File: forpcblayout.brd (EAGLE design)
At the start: 95.2 x 66.3 mm, 73 parts, among them J1 3x2 M, J2 S2B-PH-SM4-TB(LF)(SN), J3 629105136821, SW1 AYZ0202AGRLC, SW2 !RESET, T1 2N2222, T2 2N2222, T3 2N2222, T4 2N2222, U1 MCP73831, U2 MIC5219, U3 ATMEGA32U4-AUR, X2 16 MHz

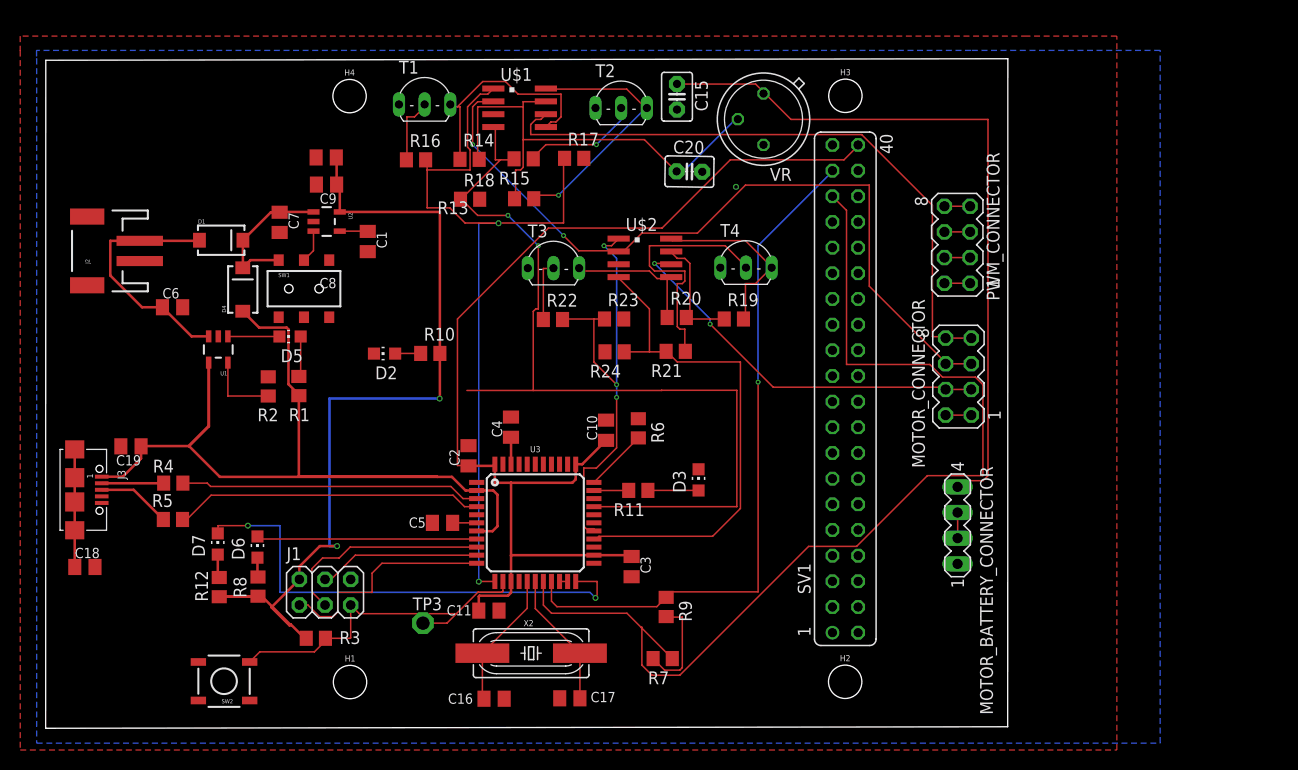
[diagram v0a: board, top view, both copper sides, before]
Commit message: Board tweaks- spacing and right angle approaches to pads
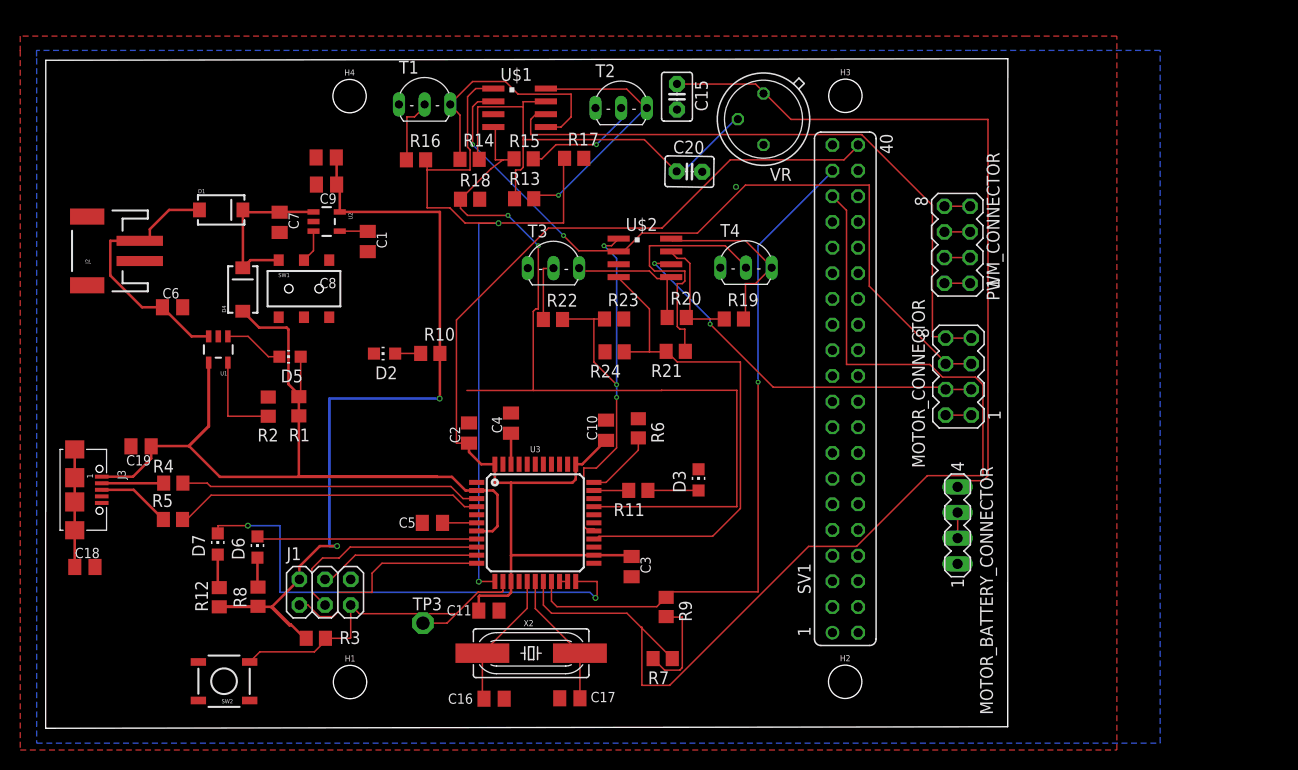
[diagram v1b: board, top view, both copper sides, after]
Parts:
- moved D1 3.00 mm to (17.4, 51.3)
- moved C2 2.25 mm to (41.9, 29.2)
- moved R2 2.00 mm to (22.0, 31.8)
- moved D5 2.00 mm to (24.2, 36.8)
- moved R1 2.00 mm to (25.1, 31.9)
- moved C19 1.00 mm to (9.44, 27.9)
- moved C5 1.00 mm to (38.3, 20.3)
- moved R12 1.00 mm to (17.2, 13.0)
- moved R8 1.00 mm to (21.0, 13.0)
- moved C4 0.40 mm to (46.0, 30.2)
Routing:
- net N$9: track 22.2 -> 25.3 mm
- net SCLK: track 104.0 -> 106.0 mm
- net MCPPROG: track 7.30 -> 9.30 mm
- net PWRIN: track 14.7 -> 16.7 mm
- net V_BATT: track 25.5 -> 27.4 mm
- net UCAP: track 2.38 -> 3.38 mm
- net N$16: track 2.33 -> 3.33 mm
- net N$15: track 1.94 -> 2.94 mm
- net N$4: track 5.11 -> 5.94 mm
- net POWER_IN: track 108.1 -> 107.4 mm
- net PWM_1: track 87.4 -> 88.1 mm
- net PE2/!HWB: track 6.23 -> 6.93 mm
- net PWM_2: track 78.5 -> 79.1 mm

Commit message: Fixed routing mistakes, extended board edge to clear matrix
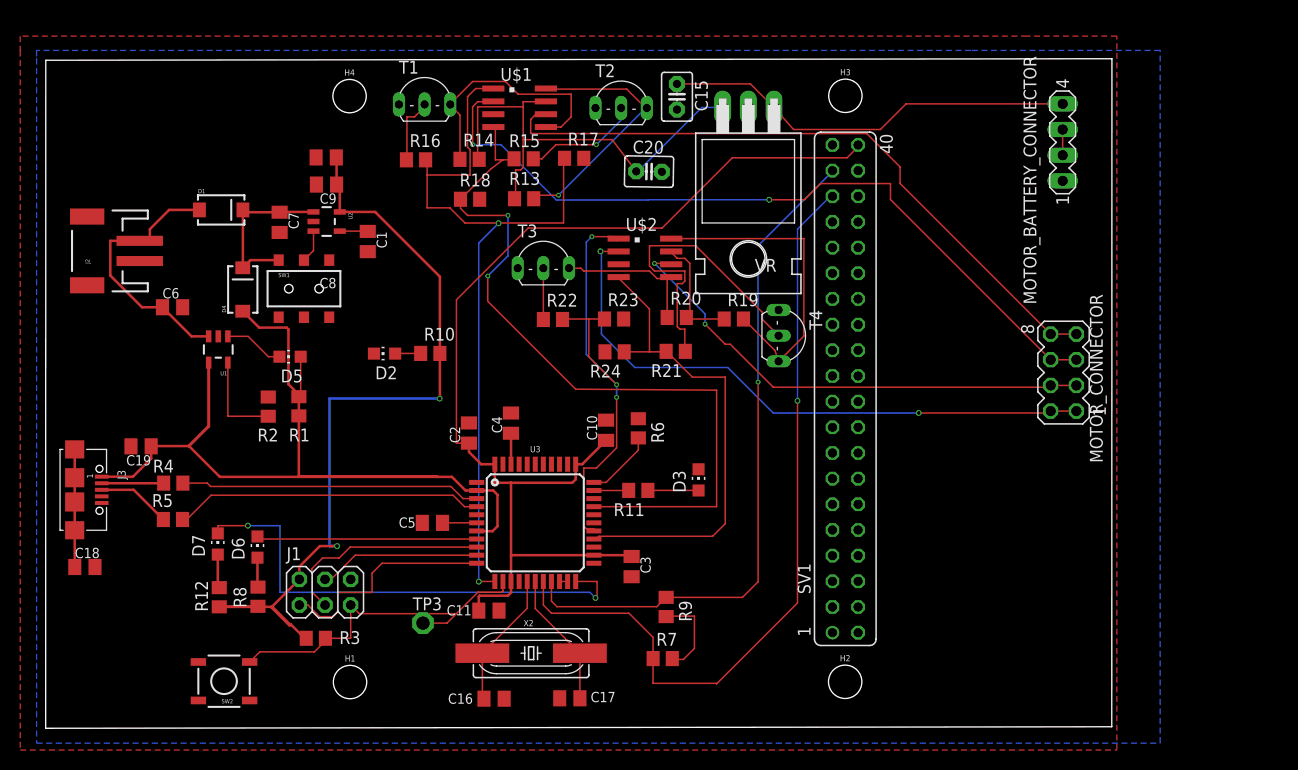
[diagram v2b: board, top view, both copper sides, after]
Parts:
- removed PWM_CONNECTOR: (no value), con-lstb:MA04-2
- VR: device linear:TO39 -> linear:TO220H
- moved MOTOR_BATTERY_CONNECTOR 39.3 mm to (100.6, 58.0)
- moved MOTOR_CONNECTOR 10.4 mm to (100.7, 35.2)
- moved T4 9.18 mm to (73.8, 38.9), turned to 270 degrees
- moved VR 9.12 mm to (69.5, 51.3)
- moved C20 4.00 mm to (59.7, 55.1)
- moved T3 1.00 mm to (49.2, 46.8)
- turned R7 to 0 degrees
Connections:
- removed net N$2: PWM_CONNECTOR.7, PWM_CONNECTOR.8
- removed net N$5: PWM_CONNECTOR.1, PWM_CONNECTOR.2
- removed net N$6: PWM_CONNECTOR.3, PWM_CONNECTOR.4
- removed net N$8: PWM_CONNECTOR.5, PWM_CONNECTOR.6
- net GND: now also VR.2; no longer VR.3
- net H_BRIDGE_POWER: now also VR.3; no longer VR.2
- net LEFT_MOTOR2: no longer U$2.2
- net RIGHT_MOTOR2: now also U$2.2
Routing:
- net RIGHT_MOTOR2: track 2.54 -> 60.7 mm, vias 0 -> 2
- net 7.4V_FROM_BATT: track 71.1 -> 41.2 mm
- net SCLK: track 106.0 -> 78.8 mm, vias 0 -> 1
- net N$18: track 18.1 -> 31.9 mm
- net PWM_1: track 88.1 -> 76.1 mm
- net RIGHT_MOTOR1: track 38.6 -> 49.2 mm
- net N$21: track 25.4 -> 31.8 mm
- net 3.3V: track 86.5 -> 82.7 mm
- net LEFT_MOTOR1: track 62.8 -> 66.3 mm
- net PWM_4: track 45.0 -> 48.2 mm
- net PWM_3: track 50.8 -> 47.8 mm
- net N$8: track 2.54 -> 0.00 mm
- net N$6: track 2.54 -> 0.00 mm
- net N$5: track 2.54 -> 0.00 mm
- net N$2: track 2.54 -> 0.00 mm
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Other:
- board size 95.2 x 66.3 mm -> 105.5 x 66.3 mm

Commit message: Added in 0ohm resistors and added in vias (for stitching)
GND Plane is still a question mark, vias don't seem to be part of flooded planes. Also DRC claims GND pins aren't connected to GND plane
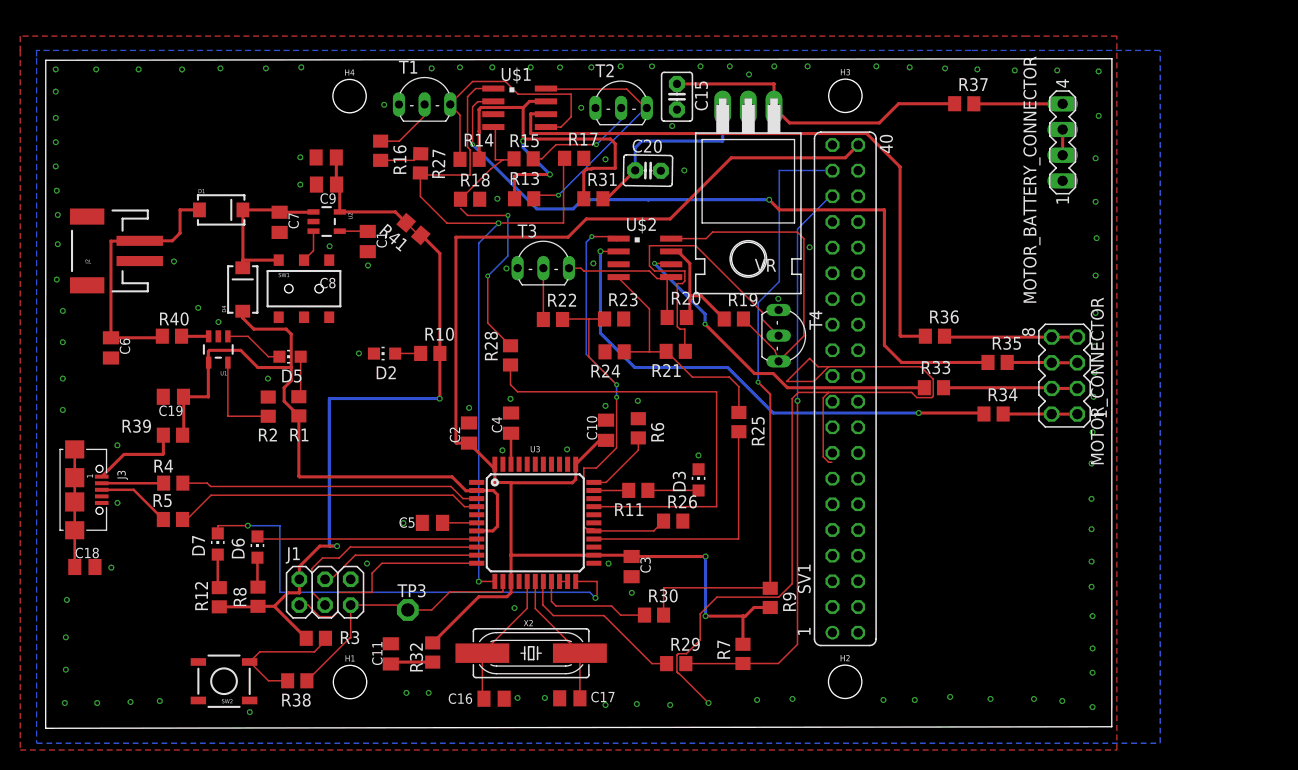
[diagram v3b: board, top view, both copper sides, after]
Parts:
- added R25, R26, R27, R28, R29, R30, R31, R32, R33, R34, R35, R36, R37, R38, R39, R40, R41: 0, rcl:R0805
- moved C11 10.6 mm to (34.2, 7.36), turned to 90 degrees
- moved R9 10.3 mm to (71.7, 12.9)
- moved R7 7.96 mm to (69.0, 7.36), turned to 90 degrees
- moved C6 7.30 mm to (6.46, 37.6), turned to 270 degrees
- moved C19 5.85 mm to (12.6, 32.8)
- moved R16 3.61 mm to (33.1, 57.1), turned to 270 degrees
- moved TP3 1.98 mm to (35.8, 11.7)
- moved MOTOR_CONNECTOR 0.32 mm to (100.8, 34.9)
- moved C20 0.14 mm to (59.6, 55.2)
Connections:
- removed net (5V@2.1A): R7.2, R9.2
- removed net H_BRIDGE_POWER: C20.1, R13.1, R14.2, U$1.7, VR.3
- removed net H_BRIDGE_POWER1: R19.1, R20.2, U$2.7
- new net 7.4_FROM_BATT: C15.1, R37.1, VR.1
- new net ACTUATOR_POWER: C20.1, R19.1, R20.2, R31.2, U$2.7, VR.3
- new net ACUATOR_POWER: R13.1, R14.2, R31.1, U$1.7
- new net N$159: J3.1, R39.2
- new net VBAT: R40.2, U1.3
- net !RESET: now also R38.1, R38.2
- net 3.3V: now also R41.1, R41.2
- net 7.4V_FROM_BATT: now also R37.2; no longer C15.1, VR.1
- net LEFT_MOTOR1: now also R36.1, R36.2
- net LEFT_MOTOR2: now also R35.1, R35.2
- net POWER_IN: now also R32.1, R32.2, R7.2, R9.2
- net PWM_1: now also R28.1, R28.2
- net PWM_2: now also R27.1, R27.2
- net PWM_3: now also R25.1, R25.2
- net PWM_4: now also R26.1, R26.2
- net RIGHT_MOTOR1: now also R33.1, R33.2
- net RIGHT_MOTOR2: now also R34.1, R34.2
- net SCLK: now also R29.1, R29.2
- net SDA: now also R30.1, R30.2
- net VBUS: now also R39.1; no longer J3.1
- net V_BATT: now also R40.1; no longer U1.3
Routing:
- net N$99: track 0.00 -> 85.1 mm, vias 0 -> 1
- net H_BRIDGE_POWER: track 46.3 -> 0.00 mm
- net ACUATOR_POWER: track 0.00 -> 44.2 mm, vias 0 -> 2
- net POWER_IN: track 108.6 -> 144.3 mm, vias 0 -> 2
- net 7.4V_FROM_BATT: track 41.2 -> 8.79 mm
- net ACTUATOR_POWER: track 0.00 -> 31.8 mm
- net 7.4_FROM_BATT: track 0.00 -> 31.2 mm
- net VBUS: track 91.5 -> 66.8 mm
- net H_BRIDGE_POWER1: track 11.8 -> 0.00 mm
- net N$159: track 0.00 -> 8.88 mm
- net (5V@2.1A): track 8.70 -> 0.00 mm
- net LEFT_MOTOR1: track 66.3 -> 73.8 mm
- net PWM_4: track 48.2 -> 55.3 mm
- net SDA: track 67.4 -> 73.2 mm
- net LEFT_MOTOR2: track 77.0 -> 81.5 mm
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
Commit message: Changed 0ohm resistors to through hole
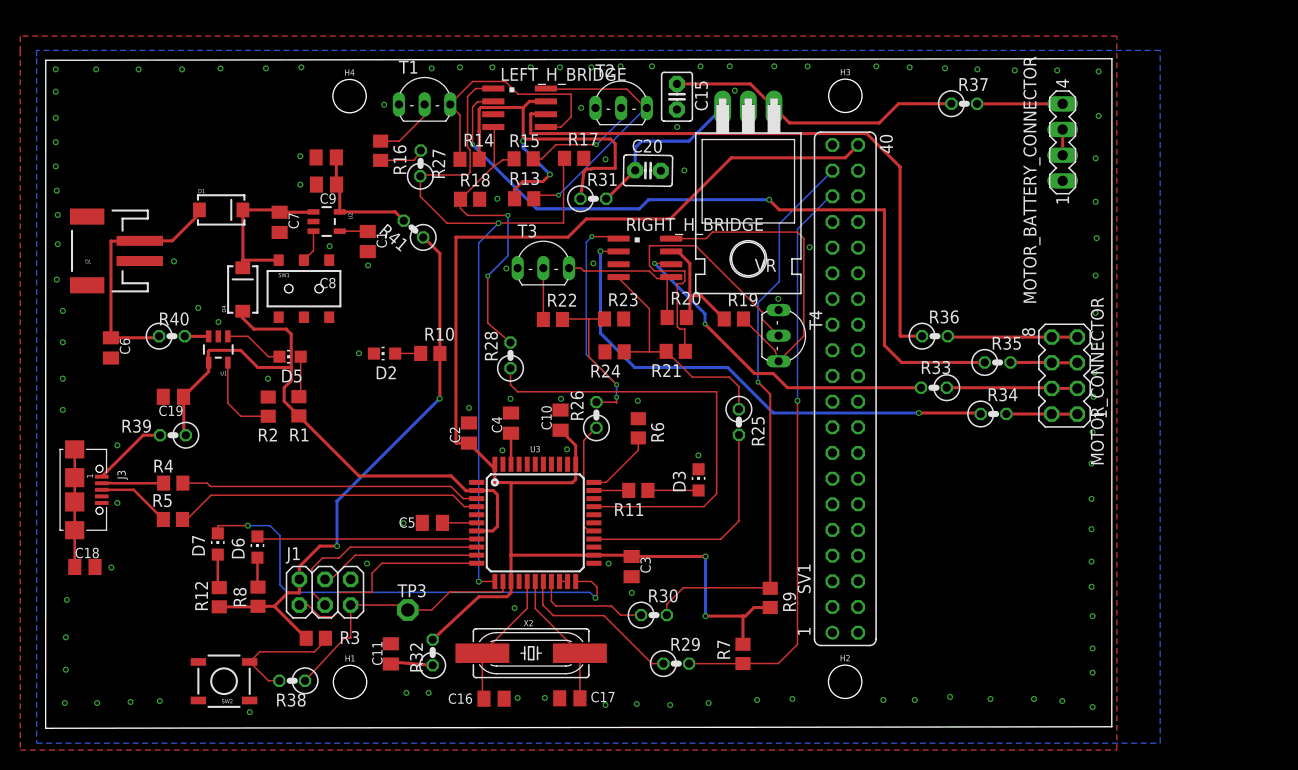
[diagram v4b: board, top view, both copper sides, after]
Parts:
- R25, R26, R27, R28, R29, R30, R31, R32, R33, R34, R35, R36, R37, R38, R39, R40, R41: device rcl:R0805 -> rcl:0207/2V
- moved R26 13.0 mm to (54.5, 31.0), turned to 90 degrees
- moved C10 4.61 mm to (51.0, 30.5)
- moved R38 0.50 mm to (24.4, 4.70)
- renumbered U$1 to LEFT_H_BRIDGE, U$2 to RIGHT_H_BRIDGE
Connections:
- removed net N$159: J3.1, R39.2
- net VBUS: now also J3.1, R39.2
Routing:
- net N$99: track 85.1 -> 0.00 mm
- net PWM_4: track 55.3 -> 46.1 mm
- net N$159: track 8.88 -> 0.00 mm
- net 3.3V: track 78.8 -> 71.6 mm
- net SDA: track 73.2 -> 68.3 mm
- net V_BATT: track 27.7 -> 24.8 mm
- net VBUS: track 66.8 -> 69.3 mm
- net ACTUATOR_POWER: track 31.8 -> 29.5 mm
- net ACUATOR_POWER: track 44.2 -> 42.4 mm
- net 7.4_FROM_BATT: track 31.2 -> 29.5 mm
- net PWM_3: track 48.7 -> 47.2 mm
- net TX_LED: track 48.9 -> 47.5 mm
- net MCPPROG: track 9.30 -> 8.54 mm
- net LEFT_MOTOR2: track 81.5 -> 80.9 mm
- net SCLK: track 74.7 -> 74.1 mm
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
